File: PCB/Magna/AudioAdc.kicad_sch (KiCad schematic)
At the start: 19 parts, among them J301 Conn_Coaxial_x2, U301 WM8782SEDS

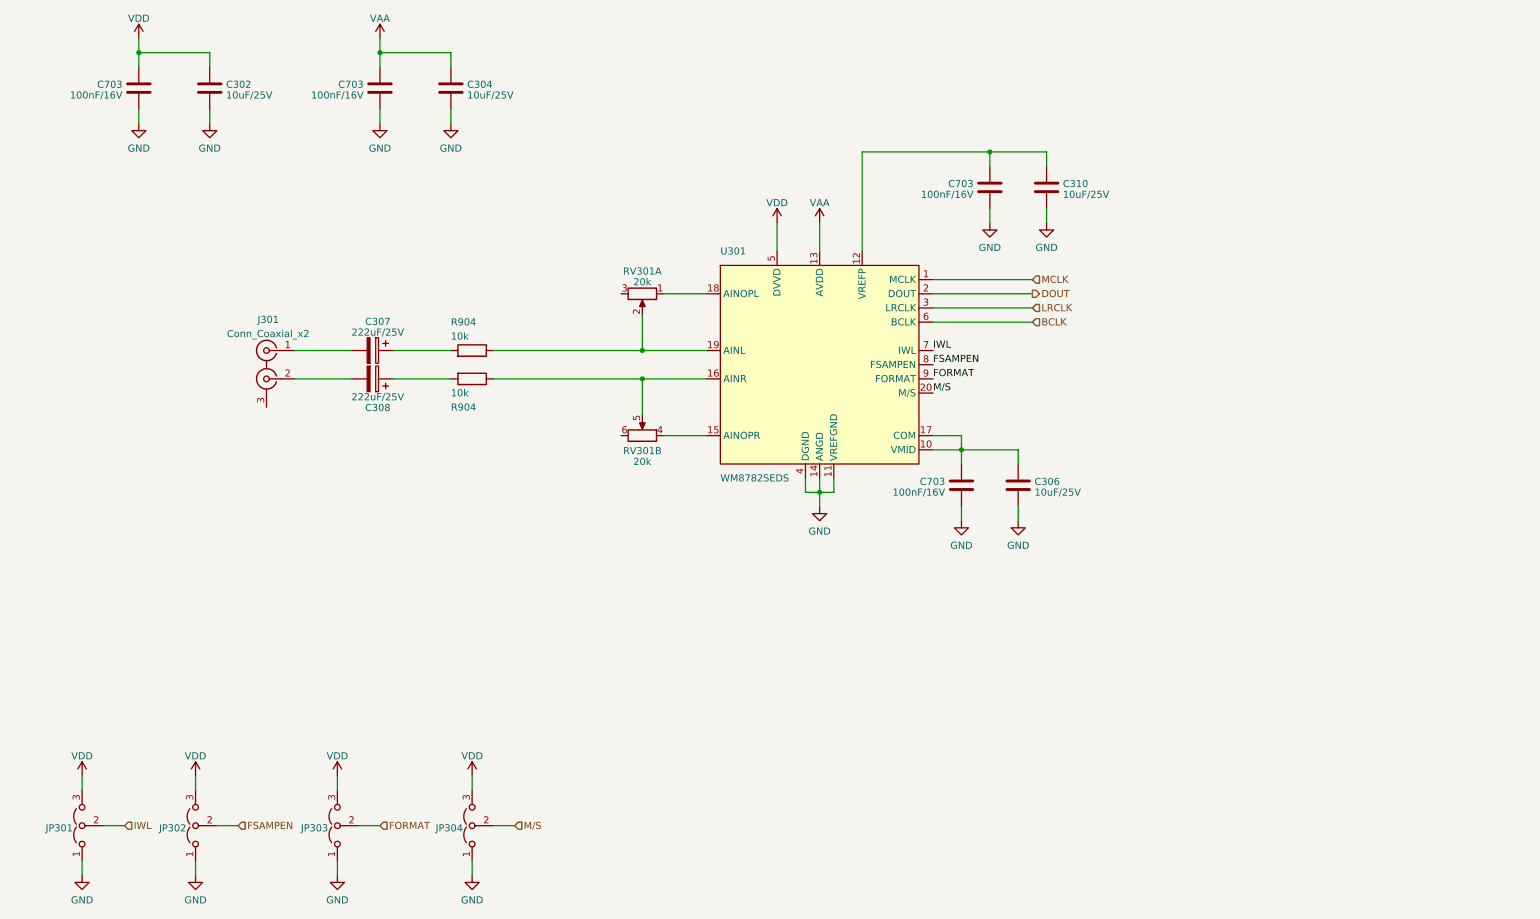
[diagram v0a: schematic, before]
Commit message: Update analogue frontend and add potentiometer interface
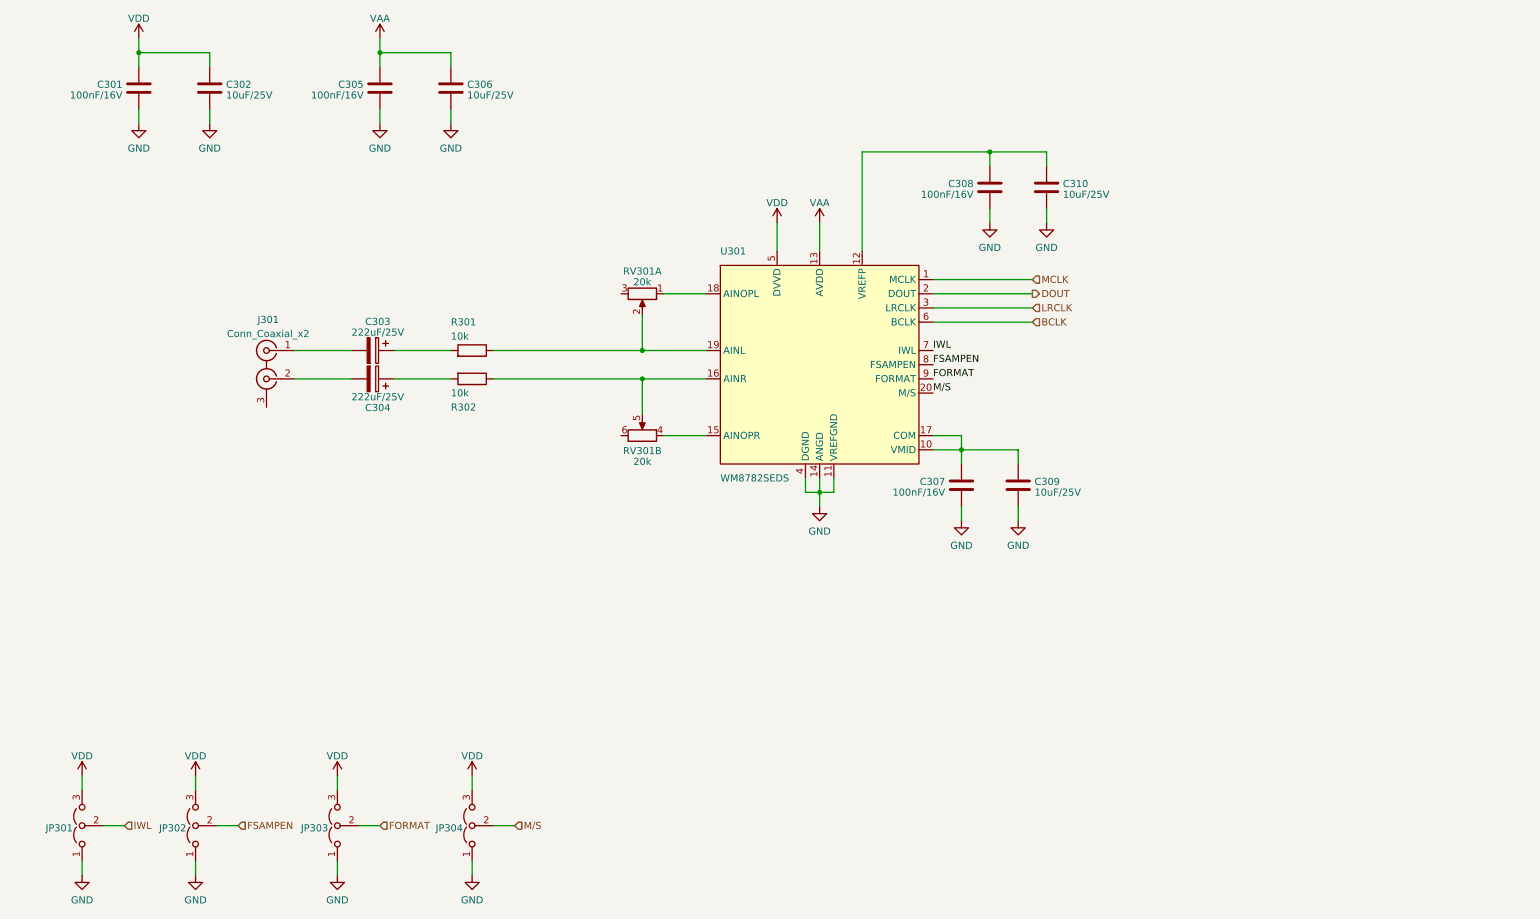
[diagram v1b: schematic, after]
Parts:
- renumbered C703 to C301, C307 to C303, C308 to C304, C703 to C305, C304 to C306, C703 to C307, C703 to C308, C306 to C309, R904 to R301, R904 to R302

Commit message: Add final touched to all schematics
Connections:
- net GND: now also J301.3 (EXT)
- no-connect marks 0 -> 2
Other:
- note added: "Decoupling Capacitors"
- moved on the sheet: C301, C302, C303, C304, C305, C306, C307, C308, C309, C310, J301, JP301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

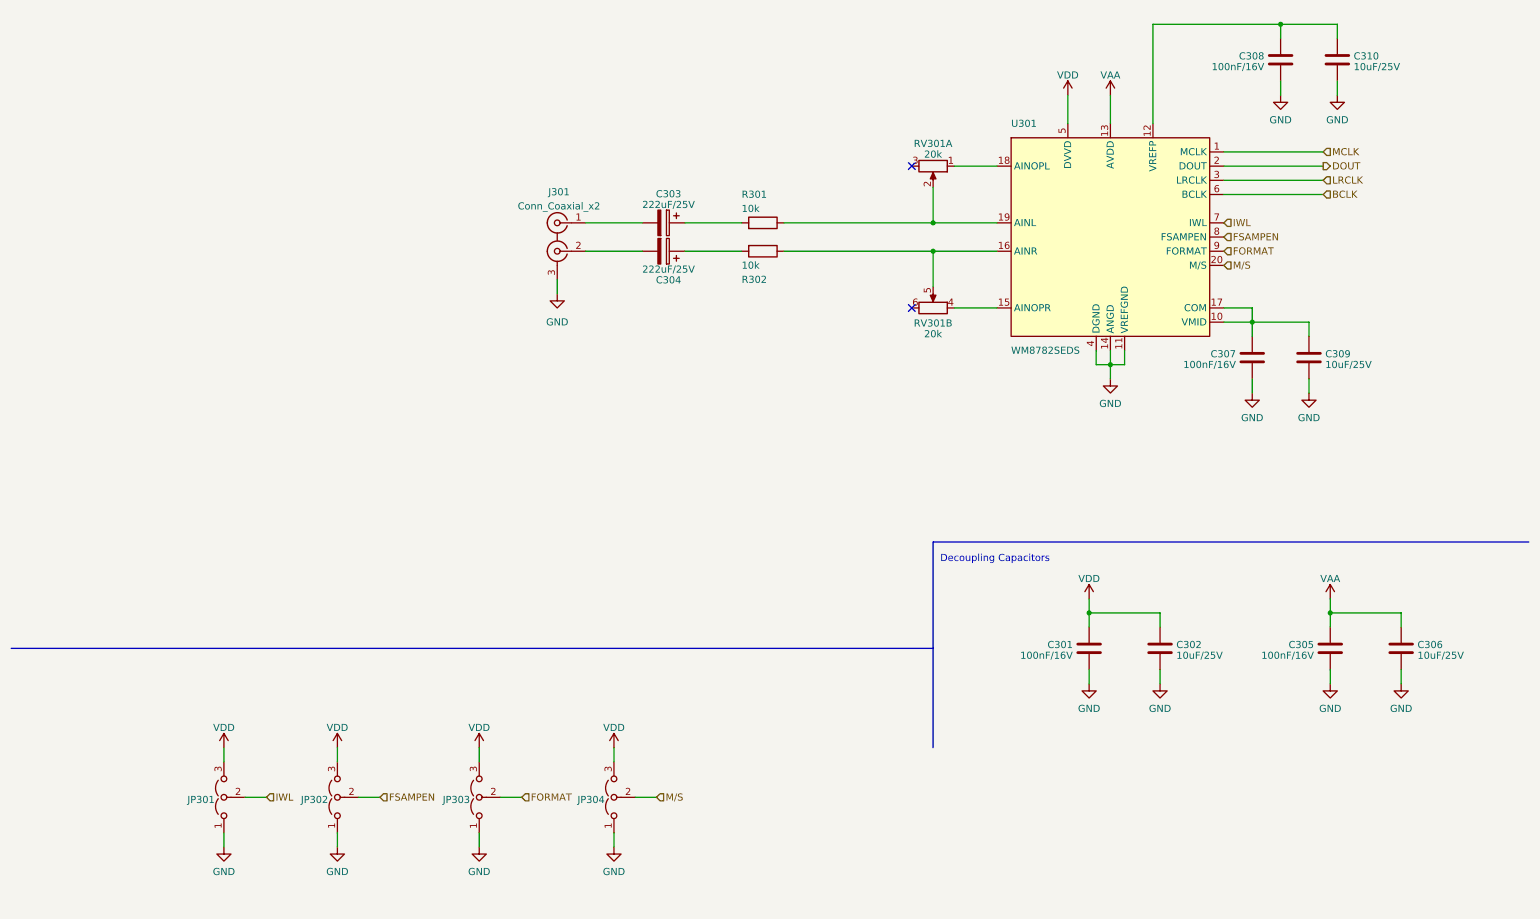
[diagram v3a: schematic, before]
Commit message: Update capacitors to parts in JLC library
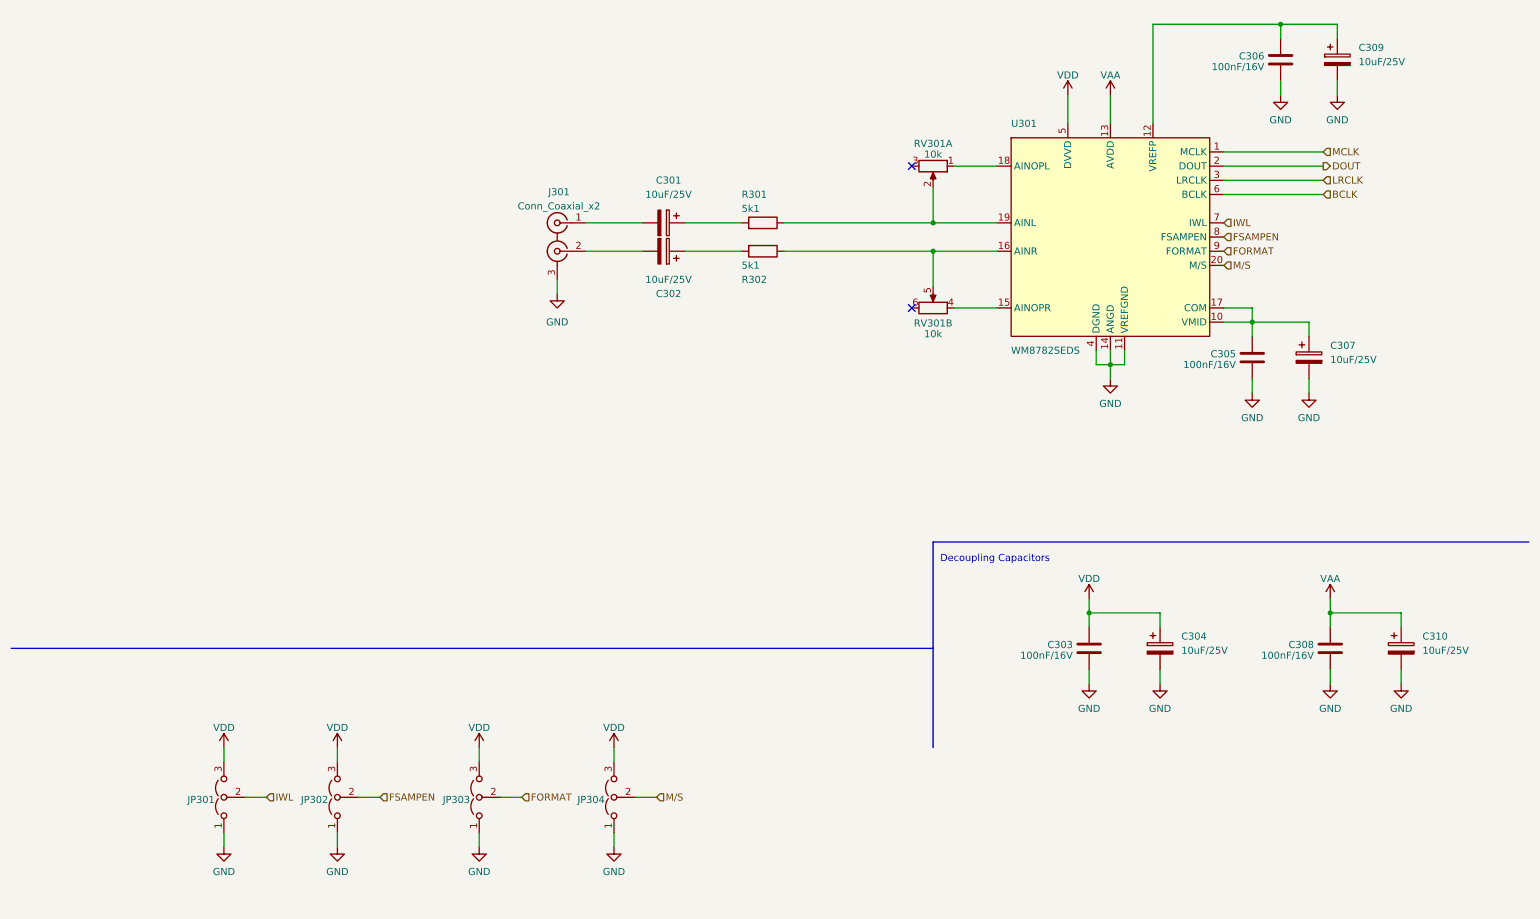
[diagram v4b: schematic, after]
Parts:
- removed C302, C306, C309, C310: 10uF/25V, Capacitor_SMD:C_0603_1608Metric, symbol Device:C
- removed C303: 222uF/25V, Capacitor_SMD:CP_Elec_8x10, symbol Device:C_Polarized
- added C301, C302, C307, C309, C310: 10uF/25V, Capacitor_SMD:CP_Elec_4x5.8, symbol Device:C_Polarized
- C303: renamed from C301; footprint Capacitor_SMD:C_0402_1005Metric -> Capacitor_SMD:C_0805_2012Metric; LCSC C1525 -> C218638
- C304: value 222uF/25V -> 10uF/25V; footprint Capacitor_SMD:CP_Elec_8x10 -> Capacitor_SMD:CP_Elec_4x5.8; LCSC C340762 -> C2163094
- C305: renamed from C307; footprint Capacitor_SMD:C_0402_1005Metric -> Capacitor_SMD:C_0805_2012Metric; LCSC C1525 -> C218638
- C306: renamed from C308; footprint Capacitor_SMD:C_0402_1005Metric -> Capacitor_SMD:C_0805_2012Metric; LCSC C1525 -> C218638
- C308: renamed from C305; footprint Capacitor_SMD:C_0402_1005Metric -> Capacitor_SMD:C_0805_2012Metric; LCSC C1525 -> C218638
- R301, R302: value 10k -> 5k1; footprint Resistor_SMD:R_0603_1608Metric -> Resistor_SMD:R_0805_2012Metric; LCSC C217687 -> C218638
- RV301: value 20k -> 10k
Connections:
- net GND: now also C304.2, C307.2, C309.2, C310.2
- net VAA: now also C310.1
- net VDD: now also C304.1
- net at R301.2: now also C301.1
- net at C305.1, U301.10 (VMID), U301.17 (COM): now also C307.1
- net at C306.1, U301.12 (VREFP): now also C309.1
- net at R302.2: now also C302.1; no longer C304.1
- net at J301.2 (IN2): now also C302.2; no longer C304.2
- net at J301.1 (IN1): now also C301.2

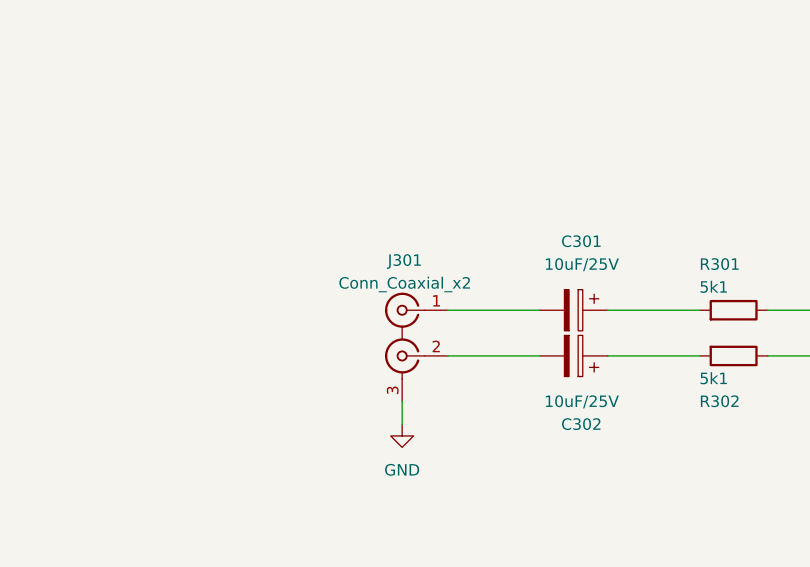
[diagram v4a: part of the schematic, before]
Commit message: Select parts for all components
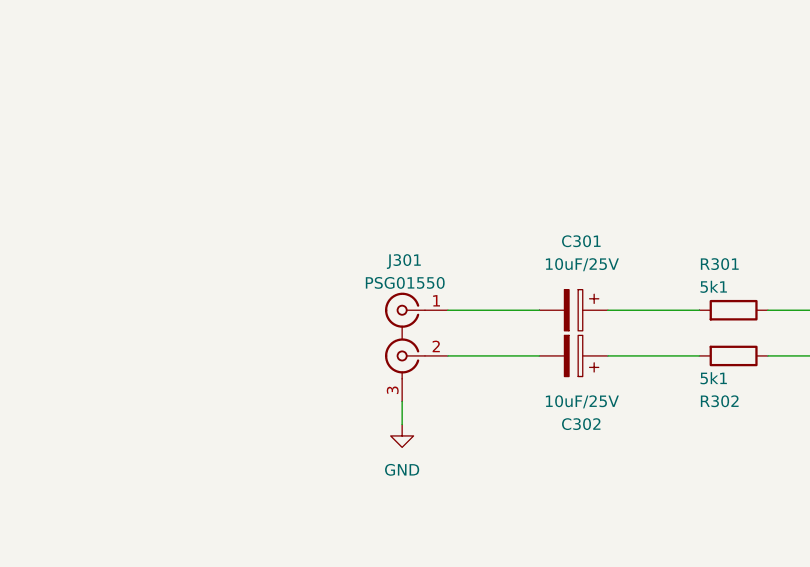
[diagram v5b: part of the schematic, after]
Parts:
- J301: value Conn_Coaxial_x2 -> PSG01550
- JP301, JP302, JP303, JP304: footprint (none) -> Jumper:SolderJumper-3_P2.0mm_Open_TrianglePad1.0x1.5mm_NumberLabels
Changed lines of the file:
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@@
       (effects (font (size 1.27 1.27)) (justify left) hide)
     )
-    (property "Footprint" "" (at 50.8 173.99 0)
+    (property "Footprint" "Jumper:SolderJumper-3_P2.0mm_Open_TrianglePad1.0x1.5mm_NumberLabels" (at 50.8 173.99 0)
       (effects (font (size 1.27 1.27)) hide)
     )
@@
       (effects (font (size 1.27 1.27)) (justify left) hide)
     )
-    (property "Footprint" "" (at 96.52 173.99 0)
+    (property "Footprint" "Jumper:SolderJumper-3_P2.0mm_Open_TrianglePad1.0x1.5mm_NumberLabels" (at 96.52 173.99 0)
       (effects (font (size 1.27 1.27)) hide)
     )
@@
       (effects (font (size 1.27 1.27)) (justify left) hide)
     )
-    (property "Footprint" "" (at 71.12 173.99 0)
+    (property "Footprint" "Jumper:SolderJumper-3_P2.0mm_Open_TrianglePad1.0x1.5mm_NumberLabels" (at 71.12 173.99 0)
       (effects (font (size 1.27 1.27)) hide)
     )
@@
       (effects (font (size 1.27 1.27)))
     )
-    (property "Value" "Conn_Coaxial_x2" (at 110.8074 68.1305 0)
+    (property "Value" "PSG01550" (at 110.8074 68.1305 0)
       (effects (font (size 1.27 1.27)))
     )
@@
       (effects (font (size 1.27 1.27)) (justify left) hide)
     )
-    (property "Footprint" "" (at 120.65 173.99 0)
-      (effects (font (size 1.27 1.27)) hide)
-    )
+    (property "Footprint" "Jumper:SolderJumper-3_P2.0mm_Open_TrianglePad1.0x1.5mm_NumberLabels" (at 120.65 173.99 0)
+      (effects (font (size 1.27 1.27)) hide)
+    )
